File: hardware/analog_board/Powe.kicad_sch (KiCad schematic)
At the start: 56 parts

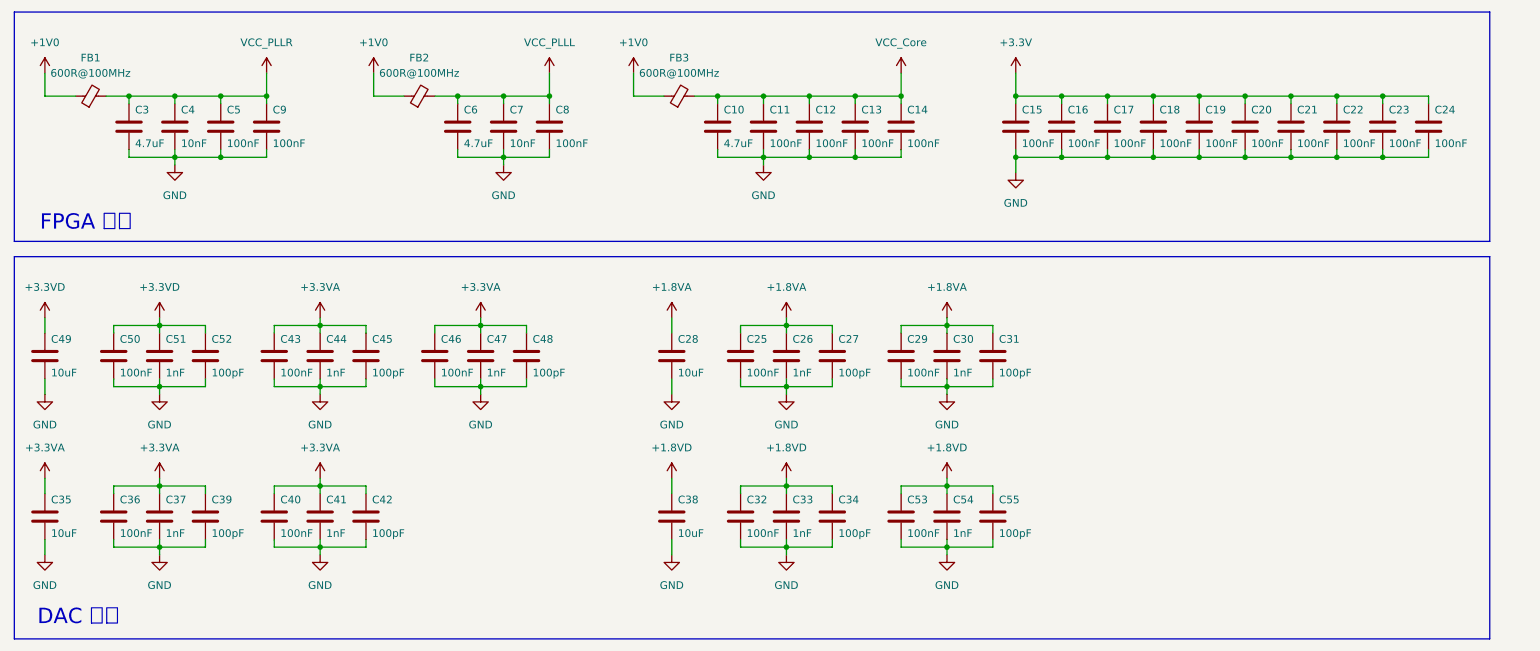
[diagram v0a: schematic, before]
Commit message: feat: 滤波器&差分转单端电路原理图
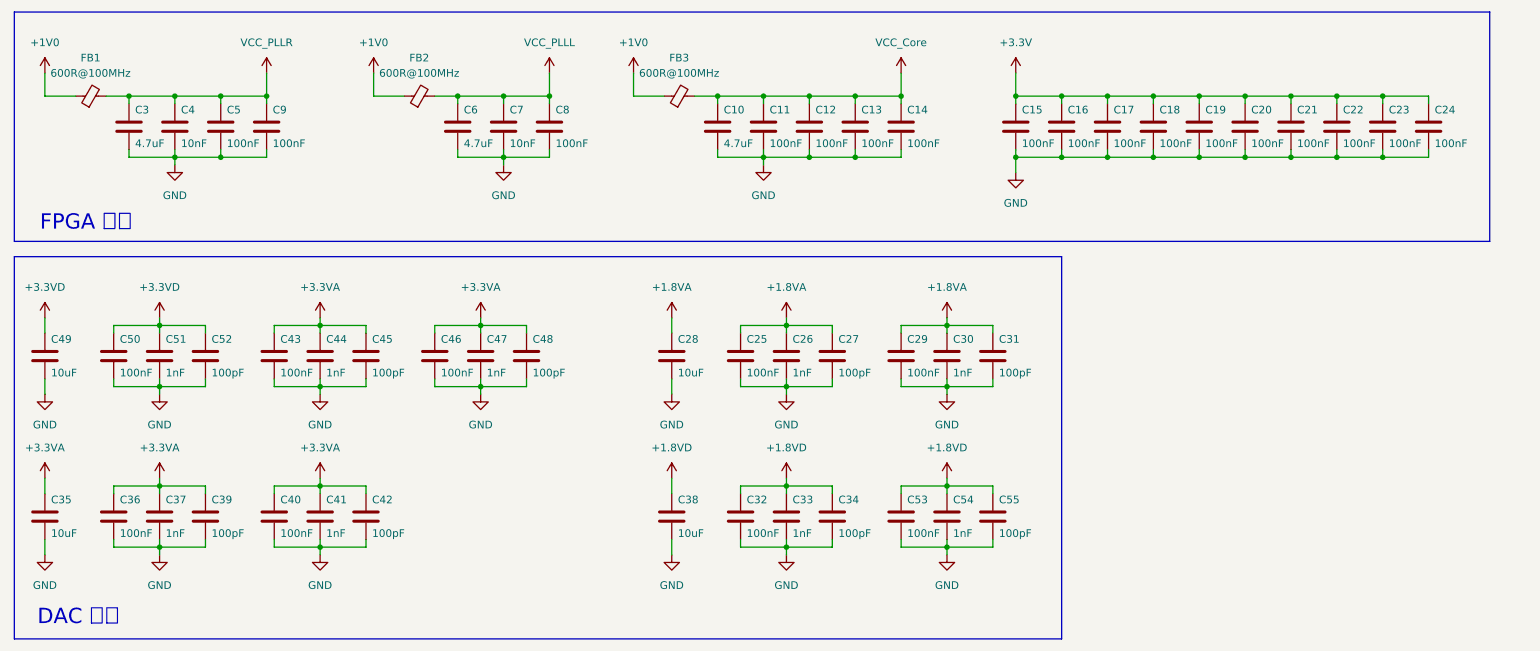
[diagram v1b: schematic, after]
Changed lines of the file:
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@@
 	(rectangle
 		(start 21.59 62.23)
-		(end 266.7 125.73)
+		(end 195.58 125.73)
 		(stroke
 			(width 0)
@@
 		)
 	)
+	(rule_area
+		(exclude_from_sim no)
+		(in_bom yes)
+		(on_board yes)
+		(dnp no)
+		(polyline
+			(pts
+				(xy 13.97 16.51) (xy 13.97 133.35) (xy 280.67 133.35) (xy 280.67 16.51)
+			)
+			(stroke
+				(width 0)
+				(type dash)
+			)
+			(fill
+				(type none)
+			)
+		)
+	)
+	(netclass_flag ""
+		(length 2.54)
+		(shape round)
+		(at 15.24 16.51 0)
+		(effects
+			(font
+				(size 1.27 1.27)
+			)
+			(justify left bottom)
+		)
+		(property "网络类" "POWER"
+			(at 15.9385 13.97 0)
+			(show_name no)
+			(do_not_autoplace no)
+			(effects
+				(font
+					(size 1.27 1.27)
+				)
+				(justify left)
+			)
+		)
+		(property "Component Class" ""
+			(at -149.86 1.27 0)
+			(show_name no)
+			(do_not_autoplace no)
+			(effects
+				(font
+					(size 1.27 1.27)
+					(italic yes)
+				)
+			)
+		)
+	)

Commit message: feat：时钟电路原理图
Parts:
- added C110, C113, C116, C119: 470nF, Capacitor_SMD:C_0603_1608Metric, symbol Device:C
- added C111, C114, C117, C120: 100nF, Capacitor_SMD:C_0603_1608Metric, symbol Device:C
- added C112, C115, C118, C97: 4.7uF, Capacitor_SMD:C_0603_1608Metric, symbol Device:C
- added FB11, FB12, FB13, FB14, FB15, FB16, FB17, FB4: 600R@100MHz, Inductor_SMD:L_0603_1608Metric, symbol Device:FerriteBead_Small
- FB1: value 600R@100MHz -> 120R@100MHz
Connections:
- net +1.8VA: now also FB12.1; no longer C25.2, C26.2, C27.2, C28.2, C29.2, C30.2, C31.2
- net +1.8VD: now also FB13.1; no longer C32.2, C33.2, C34.2, C38.2, C53.2, C54.2, C55.2
- net +3.3V: now also FB14.1, FB15.1, FB16.1, FB17.1, FB4.1
- net +3.3VA: now also FB11.1; no longer C35.2, C36.2, C37.2, C39.2, C40.2, C41.2, C42.2, C43.2, C44.2, C45.2, C46.2, C47.2, C48.2
- net GND: now also C110.1, C111.1, C112.1, C113.1, C114.1, C115.1, C116.1, C117.1, C118.1, C119.1, C120.1, C97.1
- net +3.3VD renamed +3.3VD_DAC
- net +3.3VD_DAC: now also FB4.2
- new net +1.8VA_DAC: C25.2, C26.2, C27.2, C28.2, C29.2, C30.2, C31.2, FB12.2
- new net +1.8VD_DAC: C32.2, C33.2, C34.2, C38.2, C53.2, C54.2, C55.2, FB13.2
- new net +3.3VA_DAC: C35.2, C36.2, C37.2, C39.2, C40.2, C41.2, C42.2, C43.2, C44.2, C45.2, C46.2, C47.2, C48.2, FB11.2
- new net Clock_V_{DDIO}: C115.2, C116.2, C117.2, FB16.2
- new net Clock_V_{DD}: C110.2, C111.2, C97.2, FB14.2
- new net Clock_V_{TCXO}: C118.2, C119.2, C120.2, FB17.2
- new net Clock_V_{VCO}: C112.2, C113.2, C114.2, FB15.2
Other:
- note added: "时钟 供电"
- moved on the sheet: C28, C35, C36, C37, C38, C39, C43, C44, C45, C49, C50, C51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
